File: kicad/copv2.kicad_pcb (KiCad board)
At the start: 2 copper layers, 30 x 42 mm, 32 parts, among them J1 Conn_02x03_Counter_Clockwise, Q1 DMP3098LSD-13, U1 ATtiny84A-SS, U2 LM393, U3 LM78M05_TO252

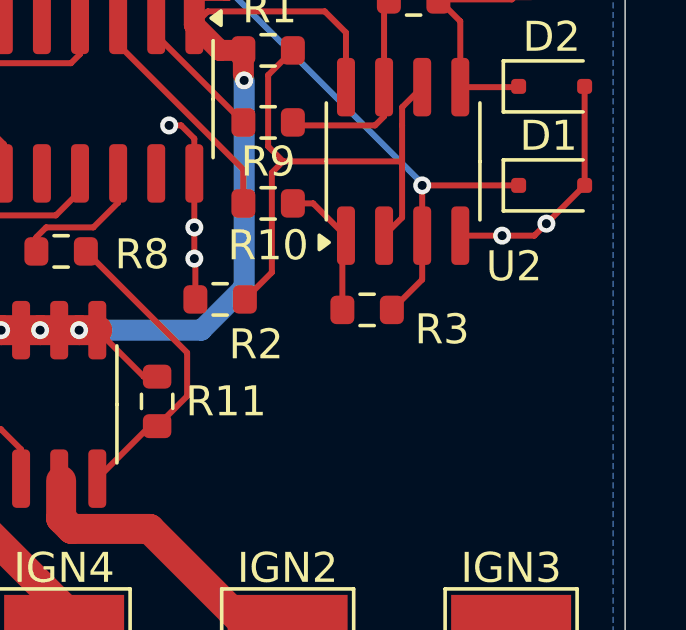
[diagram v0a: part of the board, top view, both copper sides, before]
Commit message: add cap on 2.5V
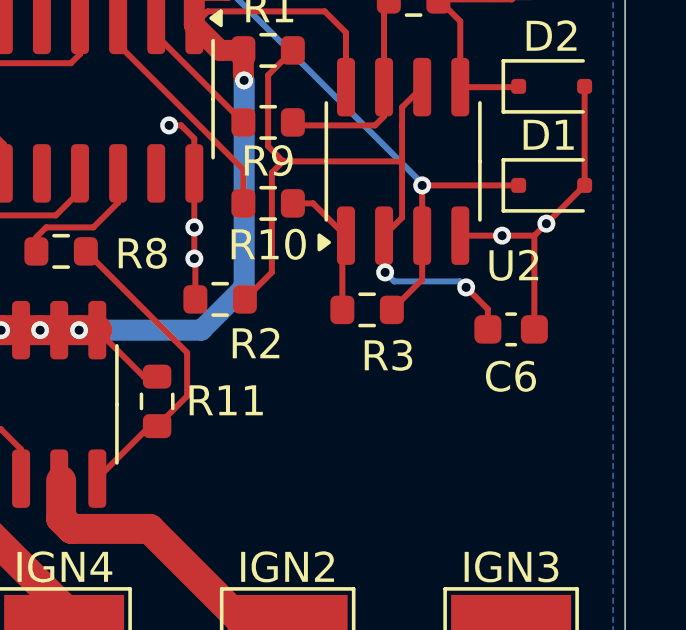
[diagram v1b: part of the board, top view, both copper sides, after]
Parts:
- added C6: 100n, Capacitor_SMD:C_0603_1608Metric, F.Cu at (142.1, 98.9)
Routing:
- net +2V5: track 19.2 -> 25.0 mm, vias 0 -> 2
- net GND: track 57.0 -> 60.1 mm

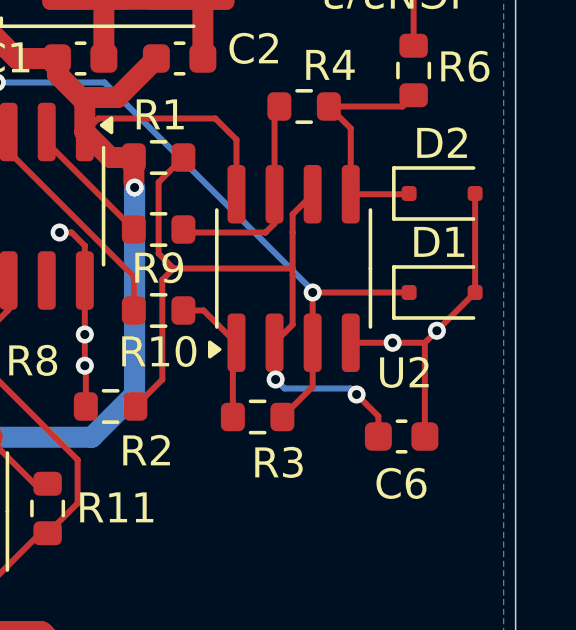
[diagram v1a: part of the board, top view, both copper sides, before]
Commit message: added vias around new capacitor
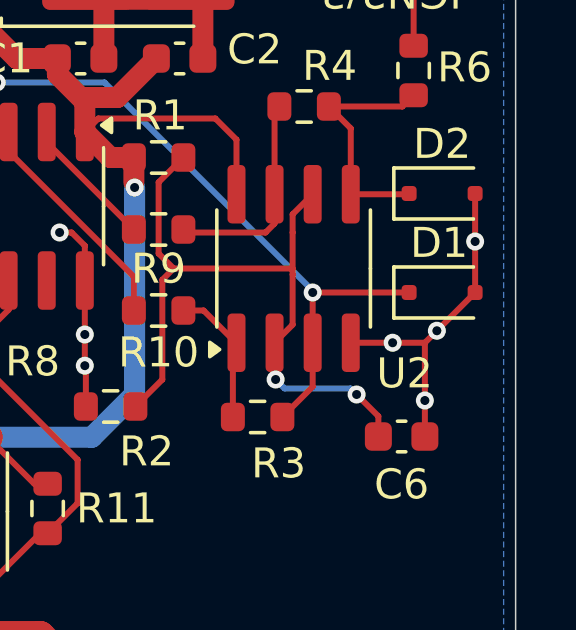
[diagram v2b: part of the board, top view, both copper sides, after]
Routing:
- net GND: vias 9 -> 11
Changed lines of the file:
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@@
+	)
+	(segment
+		(start 142.875 97.7)
+		(end 142.875 95.775)
+		(width 0.2)
+		(layer "F.Cu")
+		(net 1)
 	)
 	(segment
@@
 	(segment
 		(start 142.875 98.9)
-		(end 142.875 95.775)
+		(end 142.875 97.7)
 		(width 0.2)
 		(layer "F.Cu")
@@
 	(segment
 		(start 144.55 90.8)
-		(end 144.55 94.1)
+		(end 144.55 92.4)
 		(width 0.2)
 		(layer "F.Cu")
@@
 		(net 1)
 	)
+	(segment
+		(start 144.55 92.4)
+		(end 144.55 94.1)
+		(width 0.2)
+		(layer "F.Cu")
+		(net 1)
+	)
+	(via
+		(at 142.875 97.7)
+		(size 0.6)
+		(drill 0.3)
+		(layers "F.Cu" "B.Cu")
+		(net 1)
+	)
 	(via
 		(at 130.7 92.1)
@@
 		(size 0.6)
 		(drill 0.3)
+		(layers "F.Cu" "B.Cu")
+		(net 1)
+	)
+	(via
+		(at 144.55 92.4)
+		(size 0.6)
+		(drill 0.3)
